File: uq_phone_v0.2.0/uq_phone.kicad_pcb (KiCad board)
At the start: 6 copper layers, 45 x 108 mm, 205 parts, among them J13 Conn_01x01, J14 Conn_01x01, J15 Conn_01x01, J16 Conn_01x01, J17 Conn_01x01, J2 124018312112A, J3 BM03B-ACHSS-GAN-TF_LF__SN_, J6 Conn_ARM_SWD_TagConnect_TC2030, J7 559092474, J8 MCS-302S-C1, J9 559092474, M1 C08-00A, Q1 MMBT3904LP-7, Q2 MMBT3904LP-7, Q3 S8050, Q4 DMP2035U-7, Q5 MMBT3904LP-7, Q6 MMBT3904LP-7, SW1 SKTAAAE010, SW10 SKTAAAE010, SW11 SKTAAAE010, SW12 SKTAAAE010, SW13 SKTAAAE010, SW14 SKTAAAE010, SW15 SKTAAAE010, SW16 SKSCLCE010, SW17 SKTAAAE010, SW18 SKTAAAE010, SW19 SKTAAAE010, SW2 SKTAAAE010, SW20 SKTAAAE010, SW21 SKTAAAE010, SW22 SKSCLCE010, SW23 SKTAAAE010, SW24 SKTAAAE010, SW25 SKTAAAE010, SW26 SKTAAAE010, SW27 SKTAAAE010, SW28 SKTAAAE010, SW29 SKTAAAE010, SW3 SKTAAAE010, SW30 SKTAAAE010, SW31 SKTAAAE010, SW32 SKTAAAE010, SW33 SKTAAAE010, SW34 SKTAAAE010, SW35 SKTAAAE010, SW36 SKTAAAE010, SW37 SKTAAAE010, SW38 SKTAAAE010, SW39 SKTAAAE010, SW4 SKTAAAE010, SW40 SKTAAAE010, SW41 SKTAAAE010, SW5 SKTAAAE010, SW6 SKSCLCE010, SW7 SKTAAAE010, SW8 SKTAAAE010, SW9 SKTAAAE010, U1 TPS62162DSGR, U10 TPD8F003DQDR, U11 LSM6DSVTR, U12 DRV2603RUNR, U13 TS3A5018RSVR, U14 NAU88C22YG, U15 TPS22964CYZPR, U17 TXU0204DTRR, U18 TXU0304DTRR, U19 TXU0104DTRR, U2 MCP73871-2CCI_ML, U20 TXU0104DTRR, U3 BQ27441DRZR-G1A, U5 TCA9509MRVHR, U6 STM32H723VGHx, U7 TPS22964CYZPR, U8 TPD3F303DQDR, U9 AZV5001RA4-7

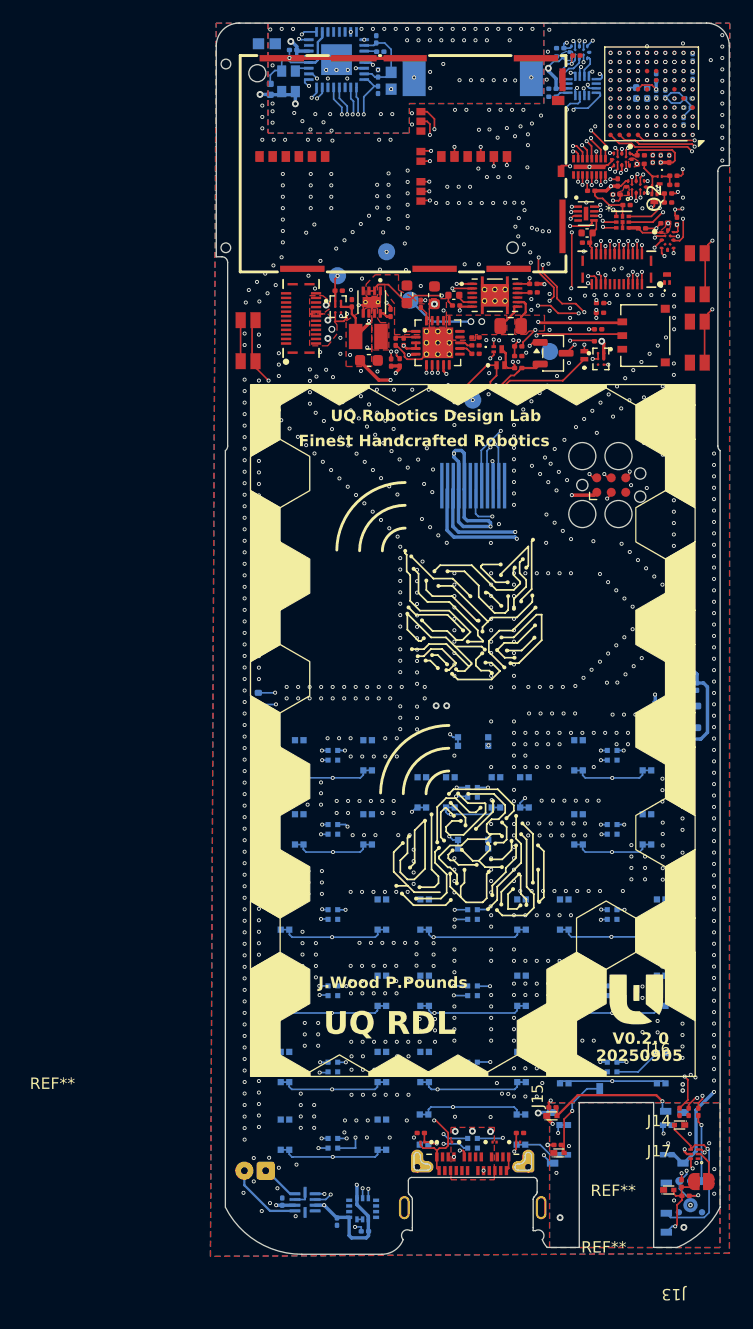
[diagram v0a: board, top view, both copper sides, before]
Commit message: Save PCB and schematic before STM32 FMC pin remapping
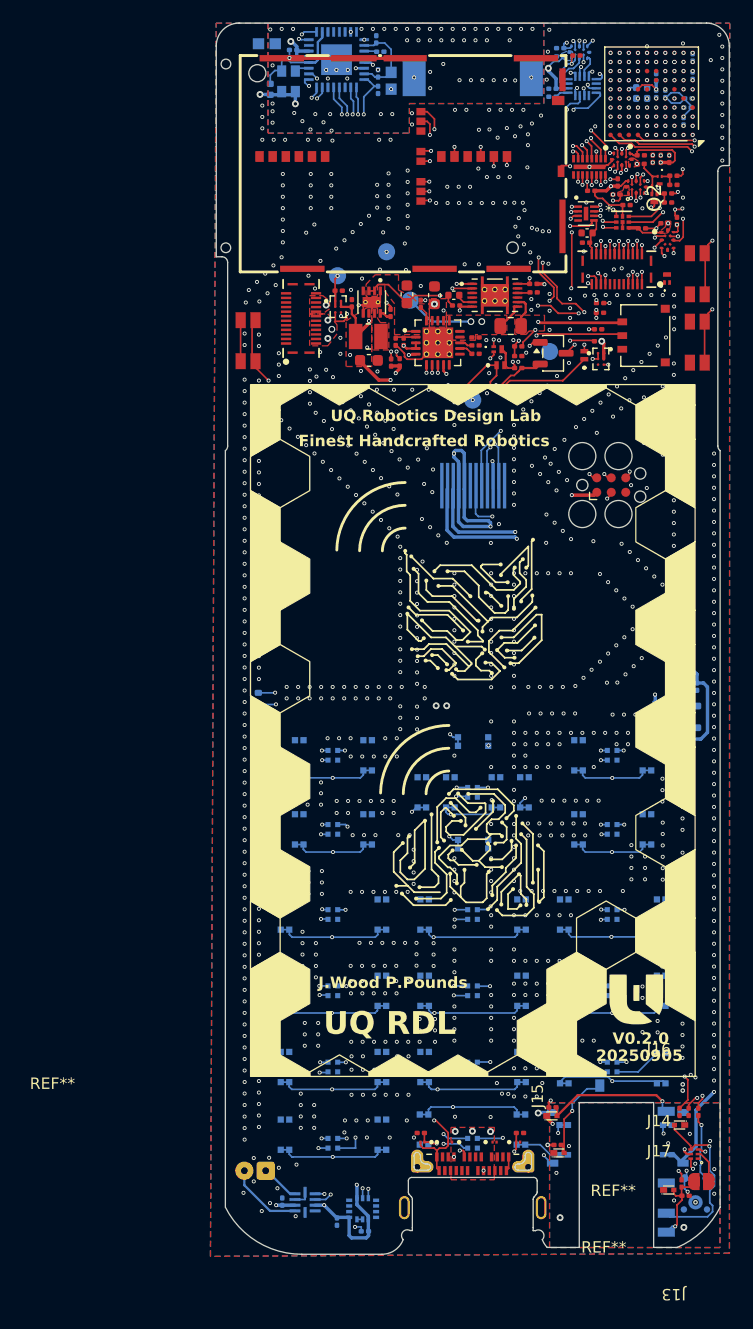
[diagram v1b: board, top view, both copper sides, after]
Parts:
- moved MK1 0.50 mm to (60.3, 123.6)
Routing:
- net MIC_BIAS: track 128.2 -> 126.0 mm
- net PB_7: track 103.3 -> 104.9 mm
- net HP_LEFT_DET: track 14.3 -> 15.2 mm

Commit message: Prototype without GPIO expander
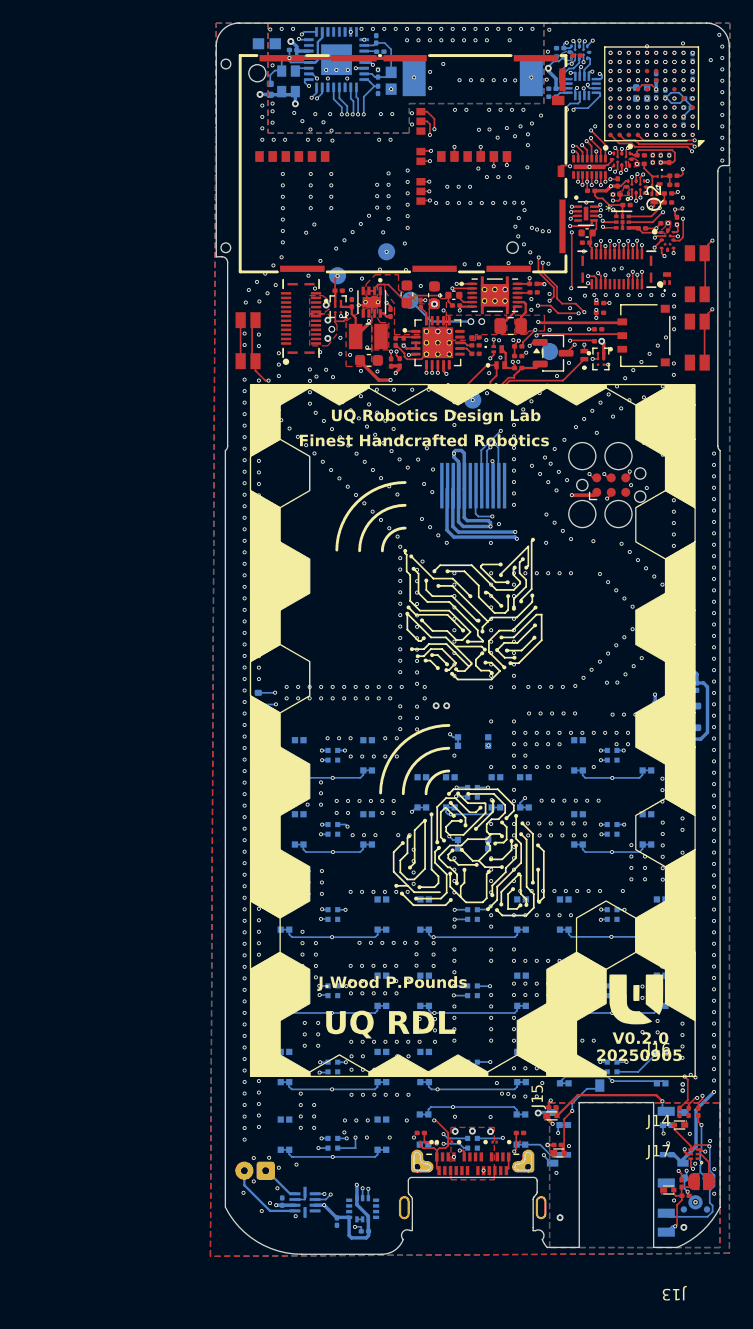
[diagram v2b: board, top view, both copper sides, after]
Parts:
- removed the REF** at (3.89, 114.4)
- removed the REF** at (53.1, 123.8)
- removed the REF** at (52.3, 128.8)
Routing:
- net MCP_OUT: track 22.6 -> 20.1 mm
